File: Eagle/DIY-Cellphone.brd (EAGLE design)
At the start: 130.8 x 58.4 mm, 66 parts, among them IC1 MEGA1284, J1 ISP, U1 MCP73831, X1 BU-SMA-V, X3 CCM03-3002 R102

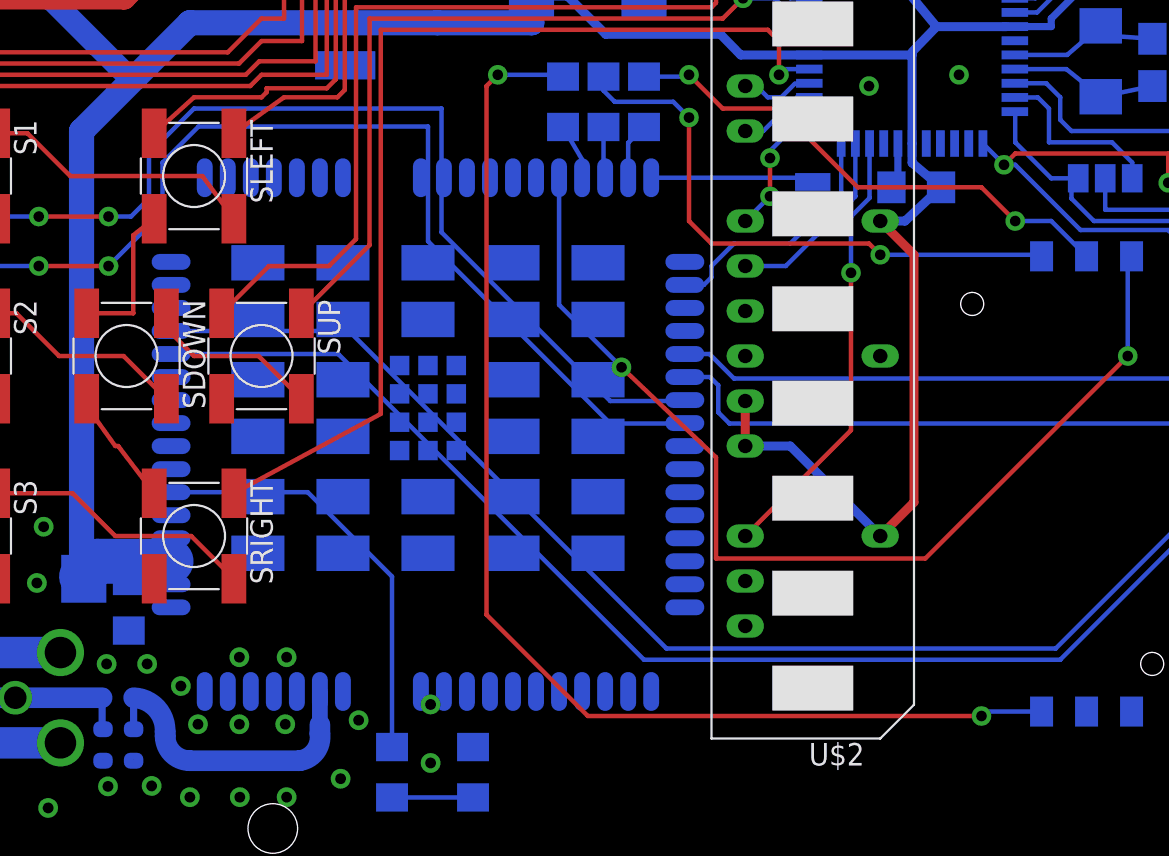
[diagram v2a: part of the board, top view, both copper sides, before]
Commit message: Re-route traces to avoid new UC15 pads.
Warning: this board still won’t work, as it’s missing level shifters
between the UC15 and the ATmega1284.
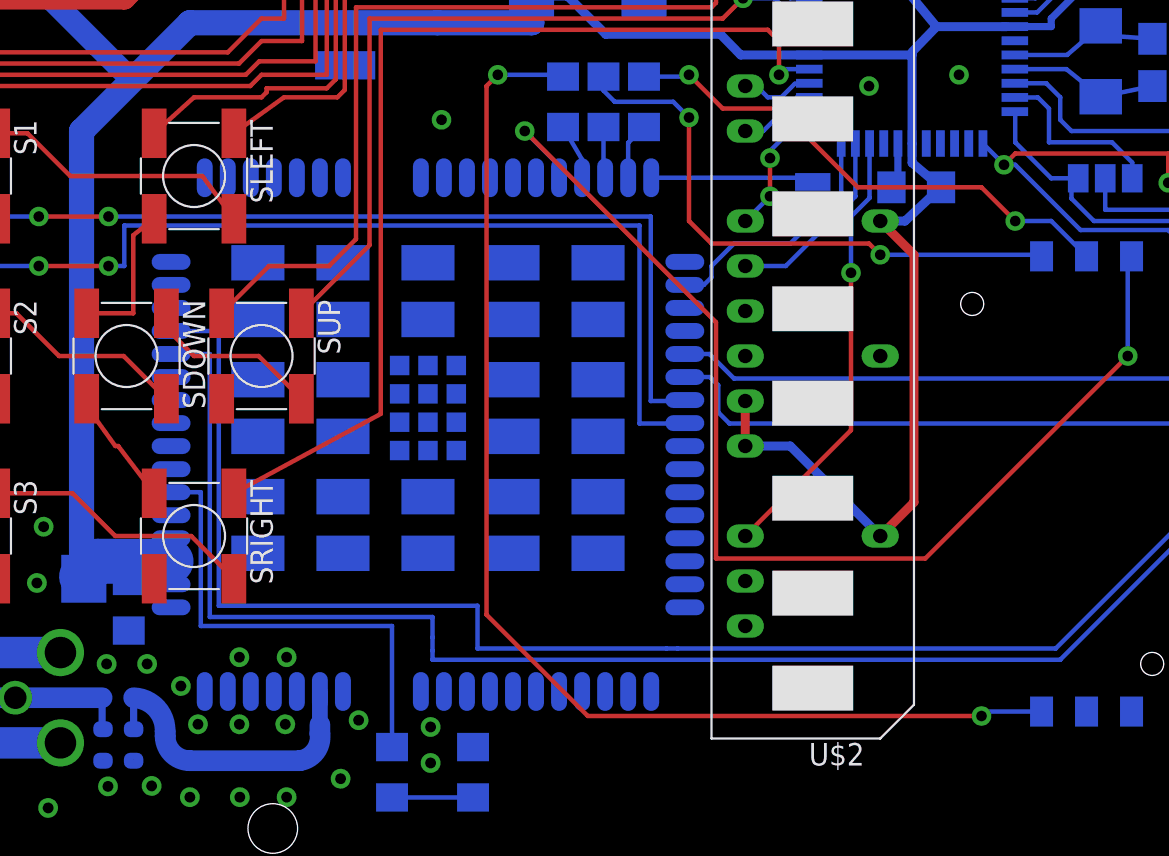
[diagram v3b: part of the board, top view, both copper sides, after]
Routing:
- net TXD1: track 118.0 -> 128.5 mm
- net RXD1: track 108.0 -> 118.1 mm
- net SIM_VDD: track 58.9 -> 65.8 mm
- net MIC1P: track 118.9 -> 114.5 mm
- net STATUS: track 24.1 -> 26.9 mm
- net MIC1N: track 117.6 -> 115.5 mm
- net GND: vias 31 -> 32

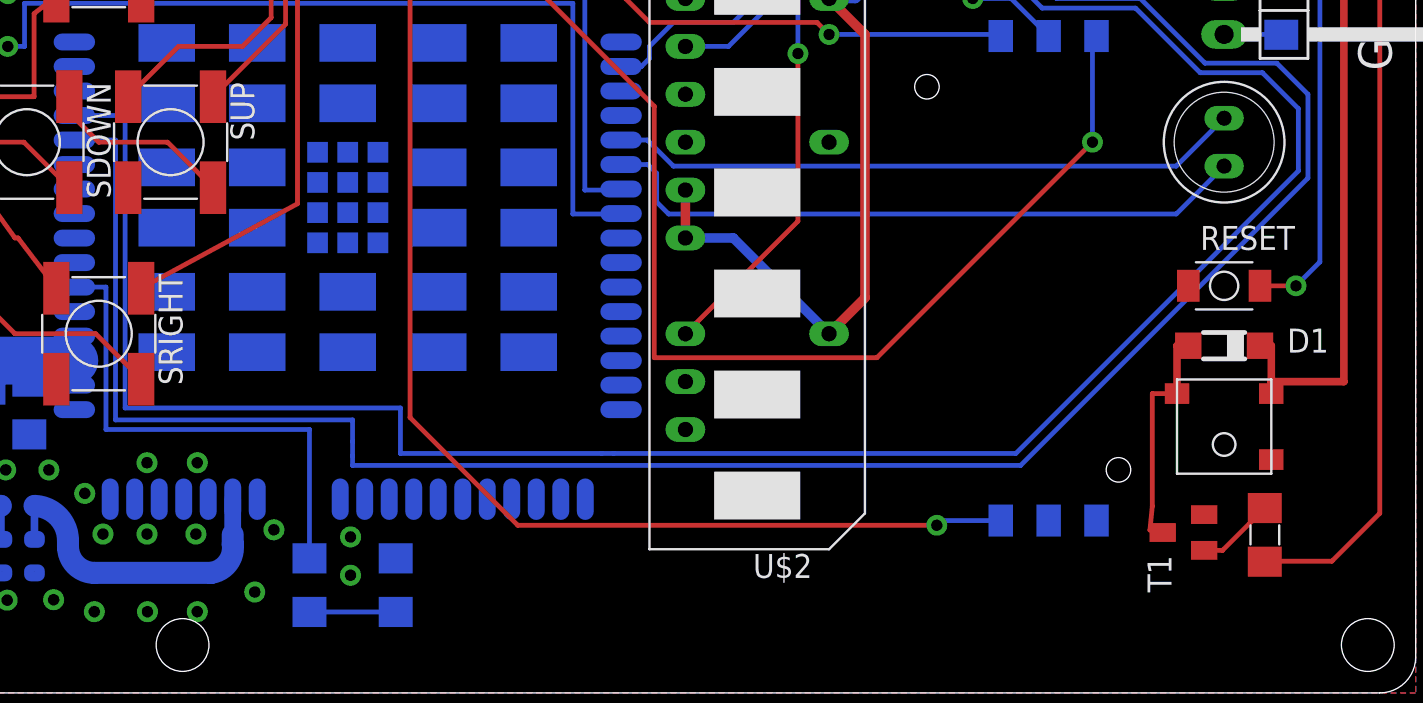
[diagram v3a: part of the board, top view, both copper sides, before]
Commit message: Add TXB0104 level shifter.
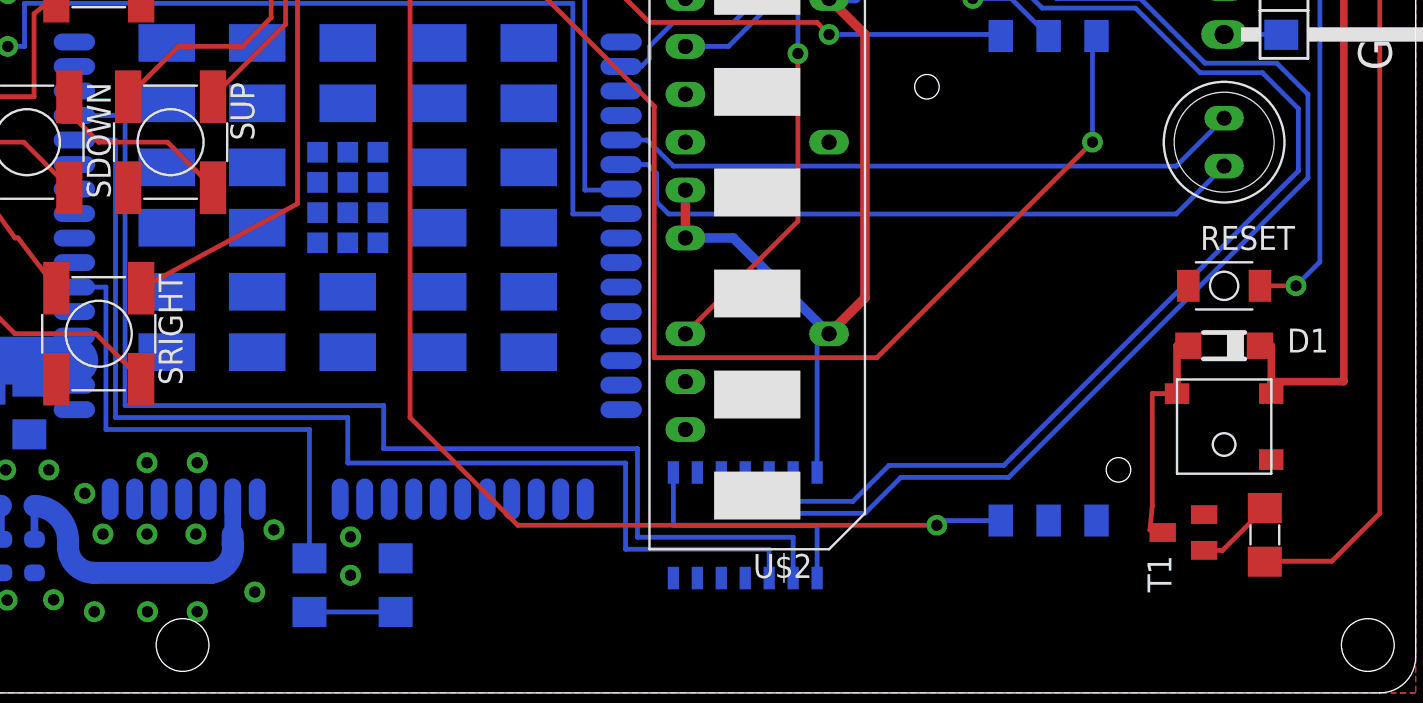
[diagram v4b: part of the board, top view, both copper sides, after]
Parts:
- added U2: (no value), SparkFun-DigitalIC:SO14
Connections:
- new net N$2: U$6.P$7, U2.1, U2.8
- new net RXD1_2.6V: U$6.P$60, U2.3
- new net TXD1_2.6V: U$6.P$61, U2.2
- net GND: now also U2.7
- net RXD1: now also U2.12; no longer U$6.P$60
- net TXD1: now also U2.13; no longer U$6.P$61
- net VCC: now also U2.14
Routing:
- net TXD1_2.6V: track 0.00 -> 62.7 mm
- net RXD1_2.6V: track 0.00 -> 60.1 mm
- net TXD1: track 128.5 -> 75.1 mm
- net RXD1: track 118.1 -> 67.2 mm
- net N$2: track 0.00 -> 13.2 mm
- net VCC: track 243.9 -> 251.9 mm
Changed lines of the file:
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@@
 <layer number="51" name="tDocu" color="7" fill="1" visible="no" active="yes"/>
 <layer number="52" name="bDocu" color="7" fill="1" visible="no" active="yes"/>
+<layer number="57" name="tCAD" color="7" fill="1" visible="no" active="no"/>
 <layer number="91" name="Nets" color="2" fill="1" visible="no" active="no"/>
 <layer number="92" name="Busses" color="1" fill="1" visible="no" active="no"/>
@@
 <layer number="97" name="Info" color="7" fill="1" visible="no" active="no"/>
 <layer number="98" name="Guide" color="6" fill="1" visible="no" active="no"/>
+<layer number="99" name="SpiceOrder" color="7" fill="1" visible="no" active="no"/>
 <layer number="100" name="Muster" color="7" fill="1" visible="no" active="no"/>
 <layer number="101" name="Patch_Top" color="7" fill="1" visible="no" active="no"/>
@@
 <layer number="106" name="bPlate" color="7" fill="1" visible="no" active="no"/>
 <layer number="107" name="Crop" color="7" fill="1" visible="no" active="no"/>
+<layer number="108" name="tplace-old" color="10" fill="1" visible="yes" active="yes"/>
+<layer number="109" name="ref-old" color="11" fill="1" visible="yes" active="yes"/>
+<layer number="110" name="fp0" color="7" fill="1" visible="yes" active="yes"/>
+<layer number="111" name="LPC17xx" color="7" fill="1" visible="yes" active="yes"/>
+<layer number="112" name="tSilk" color="7" fill="1" visible="yes" active="yes"/>
+<layer number="113" name="IDFDebug" color="7" fill="1" visible="yes" active="yes"/>
 <layer number="116" name="Patch_BOT" color="7" fill="1" visible="no" active="no"/>
 <layer number="121" name="_tsilk" color="7" fill="1" visible="no" active="no"/>
 <layer number="122" name="_bsilk" color="7" fill="1" visible="no" active="no"/>
+<layer number="123" name="tTestmark" color="7" fill="1" visible="yes" active="yes"/>
+<layer number="124" name="bTestmark" color="7" fill="1" visible="yes" active="yes"/>
 <layer number="125" name="_tNames" color="7" fill="1" visible="no" active="yes"/>
+<layer number="126" name="_bNames" color="7" fill="1" visible="yes" active="yes"/>
+<layer number="127" name="_tValues" color="7" fill="1" visible="yes" active="yes"/>
+<layer number="128" name="_bValues" color="7" fill="1" visible="yes" active="yes"/>
+<layer number="131" name="tAdjust" color="7" fill="1" visible="yes" active="yes"/>
+<layer number="132" name="bAdjust" color="7" fill="1" visible="yes" active="yes"/>
 <layer number="144" name="Drill_legend" color="7" fill="1" visible="no" active="no"/>
+<layer number="150" name="Notes" color="7" fill="1" visible="yes" active="yes"/>
 <layer number="151" name="HeatSink" color="7" fill="1" visible="no" active="no"/>
+<layer number="152" name="_bDocu" color="7" fill="1" visible="yes" active="yes"/>
+<layer number="153" name="FabDoc1" color="7" fill="1" visible="yes" active="yes"/>
+<layer number="154" name="FabDoc2" color="7" fill="1" visible="yes" active="yes"/>
+<layer number="155" name="FabDoc3" color="7" fill="1" visible="yes" active="yes"/>
+<layer number="199" name="Contour" color="7" fill="1" visible="yes" active="yes"/>
 <layer number="200" name="200bmp" color="1" fill="10" visible="no" active="no"/>
 <layer number="201" name="201bmp" color="7" fill="1" visible="no" active="no"/>
@@
 <layer number="223" name="223bmp" color="24" fill="1" visible="no" active="no"/>
 <layer number="224" name="224bmp" color="25" fill="1" visible="no" active="no"/>
+<layer number="248" name="Housing" color="7" fill="1" visible="yes" active="yes"/>
+<layer number="249" name="Edge" color="7" fill="1" visible="yes" active="yes"/>
 <layer number="250" name="Descript" color="3" fill="1" visible="no" active="no"/>
 <layer number="251" name="SMDround" color="12" fill="11" visible="no" active="no"/>
@@
 <element name="JP2" library="pinhead" package="1X04" value="" x="104.394" y="55.499"/>
 <element name="U$6" library="cellphone" package="UC15" value="UC15" x="88.665" y="39.274" rot="MR270"/>
+<element name="U2" library="SparkFun-DigitalIC" package="SO14" value="" x="95.25" y="8.89" rot="MR0">
+<attribute name="PROD_ID" value="IC-11329" x="95.25" y="8.89" size="1.778" layer="28" rot="MR0" display="off"/>
+</element>
 </elements>
 <signals>
@@
 <contactref element="U$6" pad="P$51"/>
 <contactref element="U$6" pad="P$52"/>
+<contactref element="U2" pad="14"/>
+<wire x1="99.06" y1="11.69" x2="99.06" y2="19.05" width="0.254" layer="16"/>
+<wire x1="99.06" y1="19.05" x2="99.695" y2="19.05" width="0.254" layer="16"/>
 </signal>
 <signal name="ANT" class="4">
@@
 <contactref element="U$6" pad="P$8"/>
 <via x="74.93" y="42.545" extent="1-16" drill="0.6"/>
+<contactref element="U2" pad="7"/>
 </signal>
 <signal name="DISP_DATA">
@@
 <contactref element="IC1" pad="11"/>
 <contactref element="SJ2" pad="3"/>
-<wire x1="74.422" y1="12.065" x2="109.855" y2="12.065" width="0.254" layer="16"/>
-<wire x1="109.855" y1="12.065" x2="125.095" y2="27.305" width="0.254" layer="16"/>
+<wire x1="109.22" y1="11.43" x2="125.095" y2="27.305" width="0.254" layer="16"/>
 <wire x1="125.095" y1="27.305" x2="125.095" y2="31.75" width="0.254" layer="16"/>
 <wire x1="125.095" y1="31.75" x2="123.444" y2="33.401" width="0.254" layer="16"/>
@@
 <wire x1="107.315" y1="41.275" x2="107.315" y2="42.983" width="0.254" layer="16"/>
 <wire x1="107.315" y1="42.983" x2="107.292" y2="43.006" width="0.254" layer="16"/>
-<contactref element="U$6" pad="P$60"/>
-<wire x1="59.665" y1="29.324" x2="61.849" y2="29.324" width="0.254" layer="16"/>
-<wire x1="61.849" y1="29.324" x2="61.849" y2="14.478" width="0.254" layer="16"/>
-<wire x1="61.849" y1="14.478" x2="74.422" y2="14.478" width="0.254" layer="16"/>
-<wire x1="74.422" y1="14.478" x2="74.422" y2="13.335" width="0.254" layer="16"/>
-<wire x1="74.422" y1="13.335" x2="74.422" y2="12.573" width="0.254" layer="16"/>
-<wire x1="74.422" y1="12.065" x2="74.422" y2="12.573" width="0.254" layer="16"/>
+<contactref element="U2" pad="12"/>
+<wire x1="96.52" y1="9.525" x2="96.52" y2="11.69" width="0.254" layer="16"/>
+<wire x1="96.52" y1="9.525" x2="101.6" y2="9.525" width="0.254" layer="16"/>
+<wire x1="101.6" y1="9.525" x2="103.505" y2="11.43" width="0.254" layer="16"/>
+<wire x1="103.505" y1="11.43" x2="109.22" y2="11.43" width="0.254" layer="16"/>
 </signal>
 <signal name="TXD1">
 <contactref element="IC1" pad="12"/>
 <contactref element="SJ1" pad="3"/>
-<wire x1="87.63" y1="12.7" x2="88.265" y2="12.7" width="0.254" layer="16"/>
-<wire x1="88.265" y1="12.7" x2="109.601" y2="12.7" width="0.254" layer="16"/>
-<wire x1="109.601" y1="12.7" x2="124.587" y2="27.686" width="0.254" layer="16"/>
+<wire x1="109.4105" y1="12.5095" x2="124.587" y2="27.686" width="0.254" layer="16"/>
 <wire x1="124.587" y1="27.686" x2="124.587" y2="30.988" width="0.254" layer="16"/>
 <wire x1="105.492" y1="41.206" x2="106.68" y2="40.018" width="0.254" layer="16"/>
@@
 <wire x1="110.998" y1="36.322" x2="107.315" y2="40.005" width="0.254" layer="16"/>
 <wire x1="107.315" y1="40.005" x2="106.68" y2="40.005" width="0.254" layer="16"/>
-<contactref element="U$6" pad="P$61"/>
-<wire x1="59.665" y1="30.624" x2="62.357" y2="30.624" width="0.254" layer="16"/>
-<wire x1="62.357" y1="30.624" x2="62.357" y2="15.113" width="0.254" layer="16"/>
-<wire x1="62.357" y1="15.113" x2="76.962" y2="15.113" width="0.254" layer="16"/>
-<wire x1="76.962" y1="15.113" x2="76.962" y2="12.7" width="0.254" layer="16"/>
-<wire x1="76.962" y1="12.7" x2="87.63" y2="12.7" width="0.254" layer="16"/>
+<contactref element="U2" pad="13"/>
+<wire x1="97.79" y1="11.69" x2="97.79" y2="10.16" width="0.254" layer="16"/>
+<wire x1="97.79" y1="10.16" x2="100.965" y2="10.16" width="0.254" layer="16"/>
+<wire x1="100.965" y1="10.16" x2="102.87" y2="12.065" width="0.254" layer="16"/>
+<wire x1="102.87" y1="12.065" x2="108.966" y2="12.065" width="0.254" layer="16"/>
+<wire x1="108.966" y1="12.065" x2="109.4105" y2="12.5095" width="0.254" layer="16"/>
 </signal>
 <signal name="ROW6">
@@
 <contactref element="U$6" pad="P$39"/>
 </signal>
+<signal name="RXD1_2.6V">
+<contactref element="U$6" pad="P$60"/>
+<contactref element="U2" pad="3"/>
+<wire x1="59.665" y1="29.324" x2="61.849" y2="29.324" width="0.254" layer="16"/>
+<wire x1="61.849" y1="29.324" x2="61.849" y2="14.605" width="0.254" layer="16"/>
+<wire x1="61.849" y1="14.605" x2="74.168" y2="14.605" width="0.254" layer="16"/>
+<wire x1="74.168" y1="14.605" x2="74.168" y2="12.192" width="0.254" layer="16"/>
+<wire x1="74.168" y1="12.192" x2="88.9" y2="12.192" width="0.254" layer="16"/>
+<wire x1="88.9" y1="12.192" x2="88.9" y2="7.62" width="0.254" layer="16"/>
+<wire x1="88.9" y1="7.62" x2="96.52" y2="7.62" width="0.254" layer="16"/>
+<wire x1="96.52" y1="7.62" x2="96.52" y2="6.09" width="0.254" layer="16"/>
+</signal>
+<signal name="TXD1_2.6V">
+<contactref element="U$6" pad="P$61"/>
+<contactref element="U2" pad="2"/>
+<wire x1="59.665" y1="30.624" x2="62.357" y2="30.624" width="0.254" layer="16"/>
+<wire x1="62.357" y1="30.624" x2="62.357" y2="15.24" width="0.254" layer="16"/>
+<wire x1="62.357" y1="15.24" x2="76.073" y2="15.24" width="0.254" layer="16"/>
+<wire x1="76.073" y1="15.24" x2="76.073" y2="12.954" width="0.254" layer="16"/>
+<wire x1="76.073" y1="12.954" x2="89.535" y2="12.954" width="0.254" layer="16"/>
+<wire x1="89.535" y1="12.954" x2="89.535" y2="8.255" width="0.254" layer="16"/>
+<wire x1="89.535" y1="8.255" x2="97.79" y2="8.255" width="0.254" layer="16"/>
+<wire x1="97.79" y1="8.255" x2="97.79" y2="6.09" width="0.254" layer="16"/>
+</signal>
+<signal name="N$2">
+<contactref element="U$6" pad="P$7"/>
+<contactref element="U2" pad="1"/>
+<contactref element="U2" pad="8"/>
+<wire x1="91.44" y1="11.69" x2="69.365" y2="39.274" width="0" layer="19" extent="16-16"/>
+<wire x1="99.06" y1="6.09" x2="99.06" y2="8.89" width="0.254" layer="16"/>
+<wire x1="99.06" y1="8.89" x2="91.44" y2="8.89" width="0.254" layer="16"/>
+<wire x1="91.44" y1="8.89" x2="91.44" y2="11.69" width="0.254" layer="16"/>
+</signal>
 </signals>
